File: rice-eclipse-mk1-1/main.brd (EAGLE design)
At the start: 170.1 x 119.4 mm, 197 parts, among them IC1 LMV321LICTRT, IC10 MCP6N11R, IC11 MCP6N11R, IC12 MCP6N11R, IC13 LMV321LICTRT, IC14 LMV321LICTRT, IC15 LMV321LICTRT, IC16 LMV321LICTRT, IC17 LMV321LICTRT, IC2 LMV321LICTRT, IC3 LMV321LICTRT, IC4 LMV321LICTRT, IC5 MCP6N11R, IC6 LMV321LICTRT, IC7 LMV321LICTRT, IC8 LMV321LICTRT, IC9 LMV321LICTRT, U6 1101M2S3CQE2

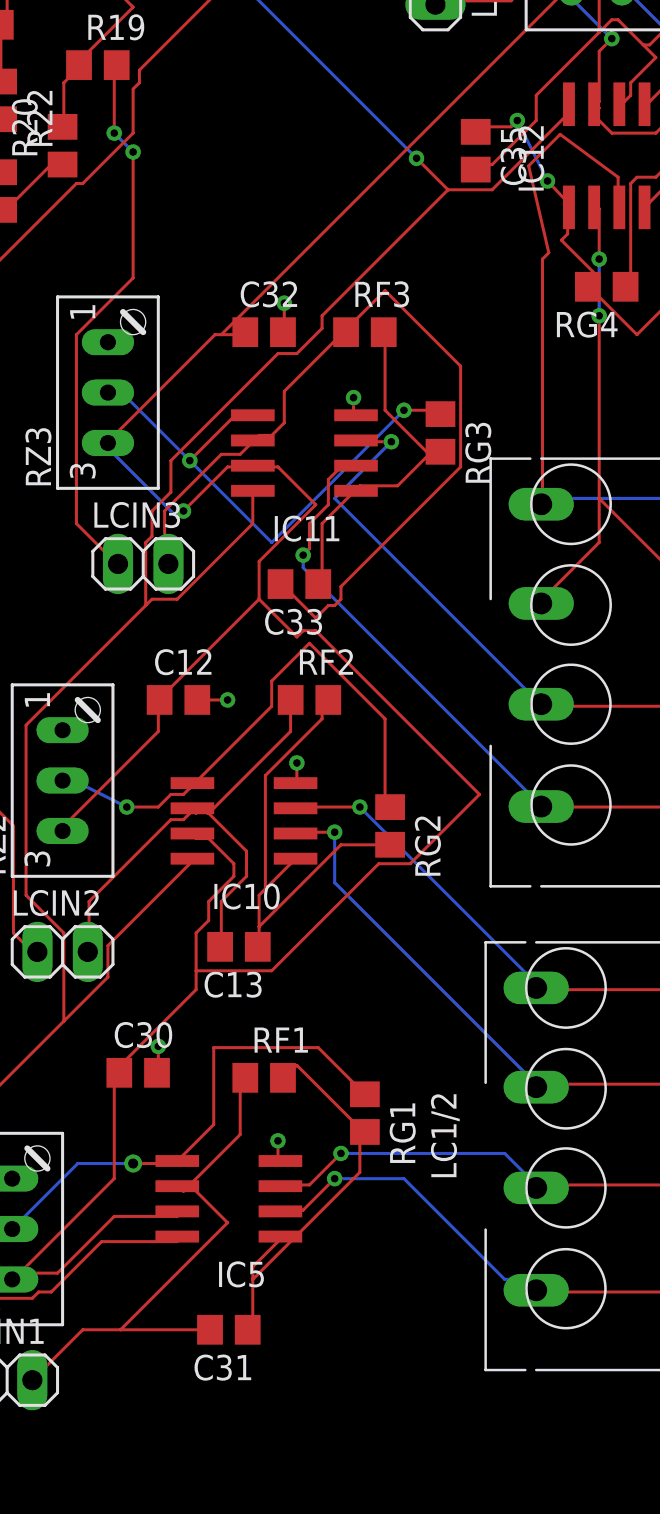
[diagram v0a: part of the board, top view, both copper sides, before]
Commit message: New schematics for Titan amp
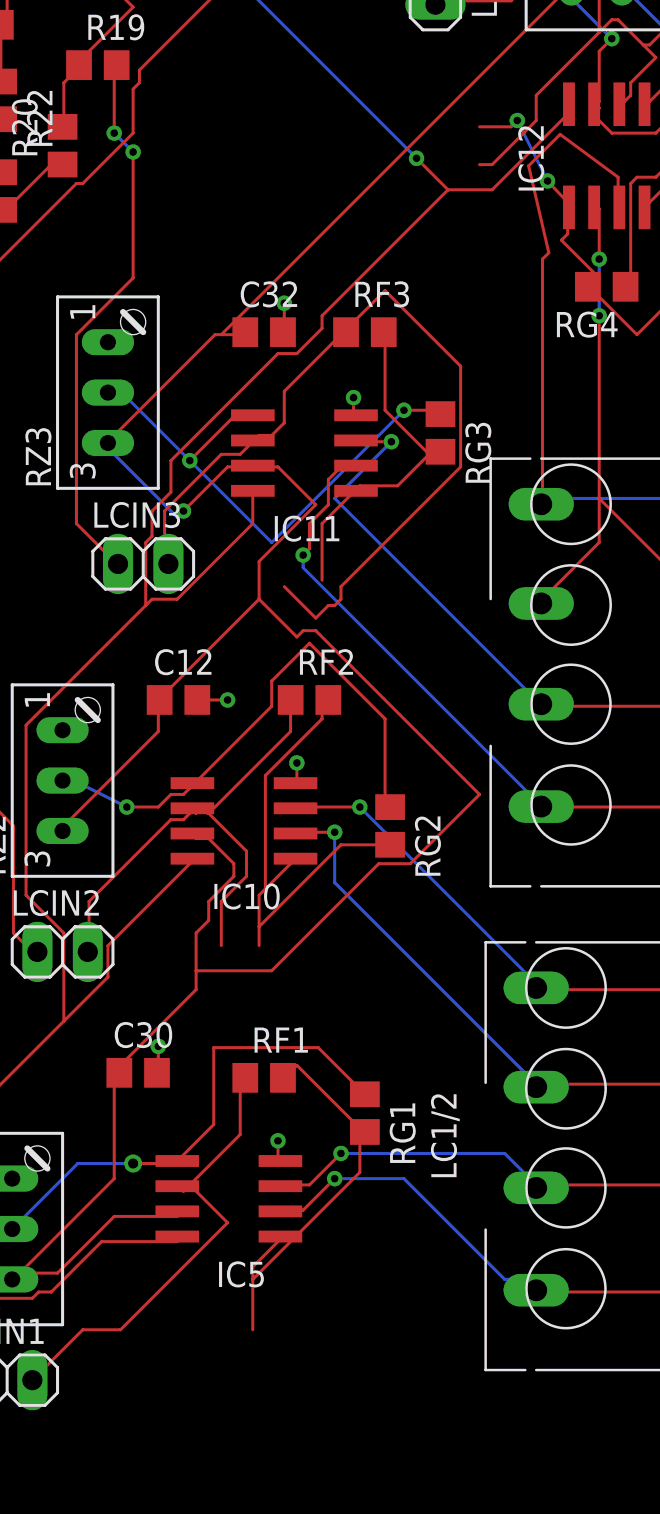
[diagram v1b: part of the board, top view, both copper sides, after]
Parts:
- removed C13, C31, C33, C35: 6.8nF, rcl:C0805
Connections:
- net LC1_PREC: no longer C31.2
- net LC2_PREC: no longer C13.2
- net LC3_PREC: no longer C33.2
- net LC4_PREC: no longer C35.2
- net N$21: no longer C13.1
- net N$39: no longer C33.1
- net N$41: no longer C31.1
- net N$46: no longer C35.1
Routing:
- net LC1_PREC: track 28.5 -> 24.0 mm
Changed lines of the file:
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@@
 <?xml version="1.0" encoding="utf-8"?>
 <!DOCTYPE eagle SYSTEM "eagle.dtd">
-<eagle version="8.7.1">
+<eagle version="8.7.0">
 <drawing>
 <settings>
-<setting alwaysvectorfont="yes"/>
+<setting alwaysvectorfont="no"/>
 <setting keepoldvectorfont="yes"/>
 <setting verticaltext="up"/>
@@
 </element>
 <element name="RZ1" library="pot" library_urn="urn:adsk.eagle:library:331" package="S64W" package3d_urn="urn:adsk.eagle:package:22708/1" value="" x="129.794" y="15.24" rot="R90"/>
-<element name="C31" library="rcl" library_urn="urn:adsk.eagle:library:334" package="C0805" package3d_urn="urn:adsk.eagle:package:23617/2" value="6.8nF" x="139.446" y="10.16" rot="R180">
-<attribute name="SPICEPREFIX" value="C" x="139.446" y="10.16" size="1.778" layer="27" rot="R180" display="off"/>
-</element>
 <element name="JP4" library="pinhead" library_urn="urn:adsk.eagle:library:325" package="1X02" package3d_urn="urn:adsk.eagle:package:22435/2" value="" x="120.396" y="94.234"/>
 <element name="IC10" library="microchip-extra" package="SO-8" value="MCP6N11R" x="140.208" y="35.814" rot="R90">
@@
 </element>
 <element name="RZ2" library="pot" library_urn="urn:adsk.eagle:library:331" package="S64W" package3d_urn="urn:adsk.eagle:package:22708/1" value="" x="132.334" y="37.846" rot="R90"/>
-<element name="C13" library="rcl" library_urn="urn:adsk.eagle:library:334" package="C0805" package3d_urn="urn:adsk.eagle:package:23617/2" value="6.8nF" x="139.954" y="29.464" rot="R180">
-<attribute name="SPICEPREFIX" value="C" x="154.94" y="48.26" size="1.778" layer="27" rot="R180" display="off"/>
-</element>
 <element name="IC11" library="microchip-extra" package="SO-8" value="MCP6N11R" x="143.256" y="54.356" rot="R90">
 <attribute name="MF" value="" x="110.998" y="43.942" size="1.778" layer="27" rot="R90" display="off"/>
@@
 </element>
 <element name="RZ3" library="pot" library_urn="urn:adsk.eagle:library:331" package="S64W" package3d_urn="urn:adsk.eagle:package:22708/1" value="" x="134.62" y="57.404" rot="R90"/>
-<element name="C33" library="rcl" library_urn="urn:adsk.eagle:library:334" package="C0805" package3d_urn="urn:adsk.eagle:package:23617/2" value="6.8nF" x="143.002" y="47.752" rot="R180">
-<attribute name="SPICEPREFIX" value="C" x="157.988" y="66.548" size="1.778" layer="27" rot="R180" display="off"/>
-</element>
 <element name="IC12" library="microchip-extra" package="SO-8" value="MCP6N11R" x="158.496" y="69.342">
 <attribute name="MF" value="" x="148.082" y="101.6" size="1.778" layer="27" display="off"/>
@@
 </element>
 <element name="RZ4" library="pot" library_urn="urn:adsk.eagle:library:331" package="S64W" package3d_urn="urn:adsk.eagle:package:22708/1" value="" x="159.258" y="76.962"/>
-<element name="C35" library="rcl" library_urn="urn:adsk.eagle:library:334" package="C0805" package3d_urn="urn:adsk.eagle:package:23617/2" value="6.8nF" x="151.892" y="69.596" rot="R270">
-<attribute name="SPICEPREFIX" value="C" x="133.096" y="84.582" size="1.778" layer="27" rot="R270" display="off"/>
-</element>
 <element name="RPD1" library="rcl" library_urn="urn:adsk.eagle:library:334" package="R0805" value="20K" x="129.54" y="93.218" rot="R90"/>
 <element name="LC_EN/CAL" library="pinhead" library_urn="urn:adsk.eagle:library:325" package="1X02" package3d_urn="urn:adsk.eagle:package:22435/2" value="" x="125.984" y="92.964" rot="R270"/>
@@
 <contactref element="IC5" pad="1"/>
 <contactref element="RG1" pad="2"/>
-<contactref element="C31" pad="1"/>
 <contactref element="RF1" pad="2"/>
 <wire x1="142.875" y1="23.495" x2="146.05" y2="20.32" width="0.1524" layer="1"/>
@@
 <wire x1="140.6525" y1="12.7" x2="140.6525" y2="10.16" width="0.1524" layer="1"/>
 <wire x1="141.9225" y1="14.605" x2="140.6525" y2="13.335" width="0.1524" layer="1"/>
-<wire x1="140.6525" y1="10.16" x2="140.396" y2="10.16" width="0.1524" layer="1"/>
 <wire x1="141.9225" y1="14.605" x2="142.046" y2="14.859" width="0.1524" layer="1"/>
 <wire x1="146.05" y1="18.0975" x2="146.05" y2="20.0025" width="0.1524" layer="1"/>
@@
 <contactref element="IC10" pad="1"/>
 <contactref element="RG2" pad="2"/>
-<contactref element="C13" pad="1"/>
 <contactref element="RF2" pad="2"/>
 <wire x1="140.97" y1="32.0675" x2="140.97" y2="30.48" width="0.1524" layer="1"/>
@@
 <wire x1="142.5575" y1="33.655" x2="141.2875" y2="32.385" width="0.1524" layer="1"/>
 <wire x1="141.2875" y1="32.385" x2="140.97" y2="32.0675" width="0.1524" layer="1"/>
-<wire x1="140.97" y1="29.5275" x2="140.904" y2="29.464" width="0.1524" layer="1"/>
 <wire x1="142.5575" y1="33.655" x2="142.808" y2="33.909" width="0.1524" layer="1"/>
 <wire x1="145.0975" y1="34.6075" x2="147.32" y2="34.6075" width="0.1524" layer="1"/>
@@
 <contactref element="IC11" pad="1"/>
 <contactref element="RG3" pad="2"/>
-<contactref element="C33" pad="1"/>
 <contactref element="RF3" pad="2"/>
 <wire x1="144.145" y1="50.8" x2="144.145" y2="47.9425" width="0.1524" layer="1"/>
 <wire x1="145.7325" y1="52.3875" x2="144.145" y2="50.8" width="0.1524" layer="1"/>
-<wire x1="144.145" y1="47.9425" x2="143.952" y2="47.752" width="0.1524" layer="1"/>
 <wire x1="145.7325" y1="52.3875" x2="145.856" y2="52.451" width="0.1524" layer="1"/>
 <wire x1="147.32" y1="56.515" x2="147.32" y2="60.325" width="0.1524" layer="1"/>
@@
 <contactref element="IC12" pad="1"/>
 <contactref element="RG4" pad="2"/>
-<contactref element="C35" pad="1"/>
 <contactref element="RF4" pad="2"/>
 <wire x1="153.67" y1="70.8025" x2="152.0825" y2="70.8025" width="0.1524" layer="1"/>
@@
 <wire x1="155.5115" y1="68.072" x2="153.9875" y2="71.12" width="0.1524" layer="16"/>
 <wire x1="156.5275" y1="66.9925" x2="155.5115" y2="68.072" width="0.1524" layer="1"/>
-<wire x1="152.0825" y1="70.8025" x2="151.892" y2="70.546" width="0.1524" layer="1"/>
 <wire x1="156.5275" y1="66.9925" x2="156.591" y2="66.742" width="0.1524" layer="1"/>
 <wire x1="160.02" y1="60.325" x2="157.7975" y2="62.5475" width="0.1524" layer="1"/>
@@
 <signal name="LC1_PREC">
 <contactref element="IC5" pad="6"/>
-<contactref element="C31" pad="2"/>
 <contactref element="RF1" pad="1"/>
 <contactref element="LCIN1" pad="2"/>
@@
 <wire x1="137.16" y1="17.145" x2="136.846" y2="17.399" width="0.1524" layer="1"/>
 <wire x1="132.08" y1="10.16" x2="133.985" y2="10.16" width="0.1524" layer="1"/>
-<wire x1="133.985" y1="10.16" x2="138.496" y2="10.16" width="0.1524" layer="1"/>
 <wire x1="129.54" y1="7.62" x2="132.08" y2="10.16" width="0.1524" layer="1"/>
 <wire x1="139.3825" y1="15.5575" x2="137.4775" y2="17.4625" width="0.1524" layer="1"/>
@@
 <contactref element="LCIN2" pad="2"/>
 <contactref element="IC10" pad="6"/>
-<contactref element="C13" pad="2"/>
 <contactref element="RF2" pad="1"/>
 <wire x1="139.065" y1="31.75" x2="139.065" y2="29.5275" width="0.1524" layer="1"/>
@@
 <wire x1="138.43" y1="36.195" x2="140.335" y2="34.29" width="0.1524" layer="1"/>
 <wire x1="137.795" y1="36.195" x2="138.1125" y2="36.5125" width="0.1524" layer="1"/>
-<wire x1="139.065" y1="29.5275" x2="139.004" y2="29.464" width="0.1524" layer="1"/>
 <wire x1="137.795" y1="36.195" x2="137.608" y2="36.449" width="0.1524" layer="1"/>
 <wire x1="142.5575" y1="40.3225" x2="142.5575" y2="41.91" width="0.1524" layer="1"/>
@@
 <contactref element="LCIN3" pad="2"/>
 <contactref element="IC11" pad="6"/>
-<contactref element="C33" pad="2"/>
 <contactref element="RF3" pad="1"/>
 <wire x1="143.8275" y1="46.0375" x2="142.24" y2="47.625" width="0.1524" layer="1"/>
@@
 <wire x1="147.32" y1="62.5475" x2="151.13" y2="58.7375" width="0.1524" layer="1"/>
 <wire x1="145.415" y1="60.6425" x2="147.32" y2="62.5475" width="0.1524" layer="1"/>
-<wire x1="142.24" y1="47.625" x2="142.052" y2="47.752" width="0.1524" layer="1"/>
 <wire x1="145.415" y1="60.6425" x2="145.354" y2="60.452" width="0.1524" layer="1"/>
 <wire x1="141.605" y1="55.245" x2="140.97" y2="55.245" width="0.1524" layer="1"/>
@@
 <contactref element="LCIN4" pad="2"/>
 <contactref element="IC12" pad="6"/>
-<contactref element="C35" pad="2"/>
 <contactref element="RF4" pad="1"/>
 <wire x1="152.7175" y1="68.8975" x2="152.0825" y2="68.8975" width="0.1524" layer="1"/>
@@
 <wire x1="159.7025" y1="72.39" x2="159.7025" y2="73.025" width="0.1524" layer="1"/>
 <wire x1="159.385" y1="72.0725" x2="159.7025" y2="72.39" width="0.1524" layer="1"/>
-<wire x1="152.0825" y1="68.8975" x2="151.892" y2="68.646" width="0.1524" layer="1"/>
 <wire x1="159.385" y1="72.0725" x2="159.131" y2="71.942" width="0.1524" layer="1"/>
 <wire x1="165.1" y1="68.2625" x2="165.1" y2="67.31" width="0.1524" layer="1"/>
